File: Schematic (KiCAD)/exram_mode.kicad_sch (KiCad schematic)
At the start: 61 parts

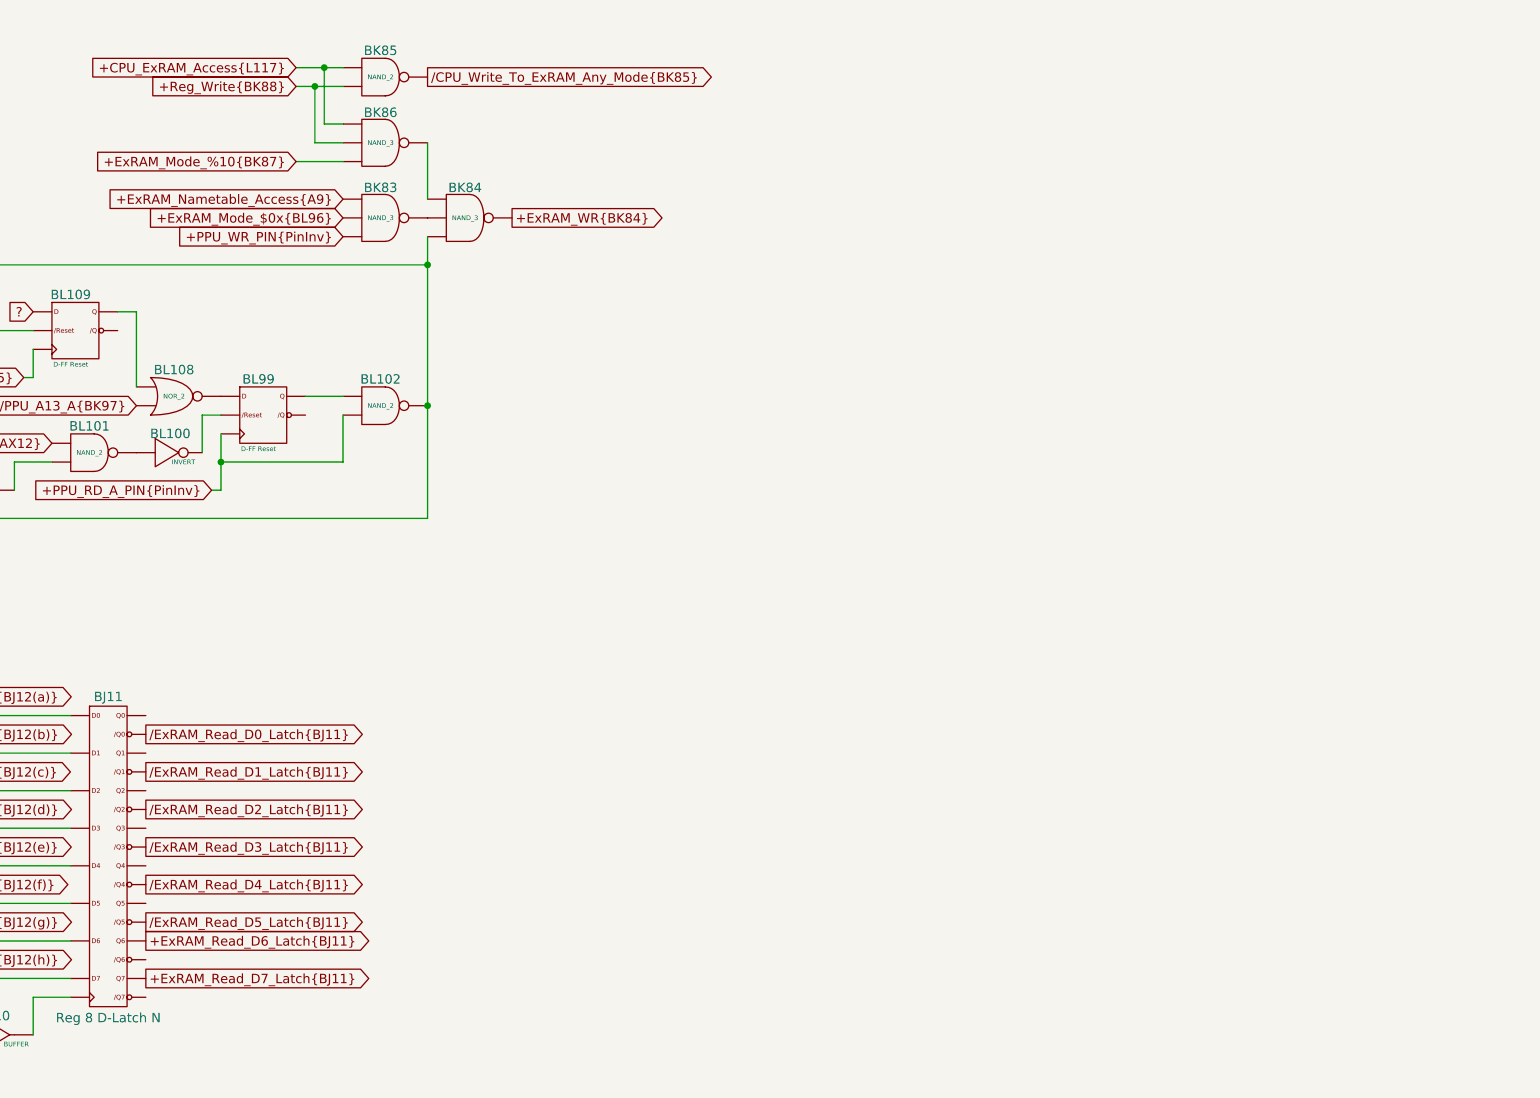
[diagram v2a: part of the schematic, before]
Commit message: - All cells in the left and center areas have now been added into the schematics.  - Changed naming of the PDF files; I was accidentally writing over furrtek's original with my new PDF.
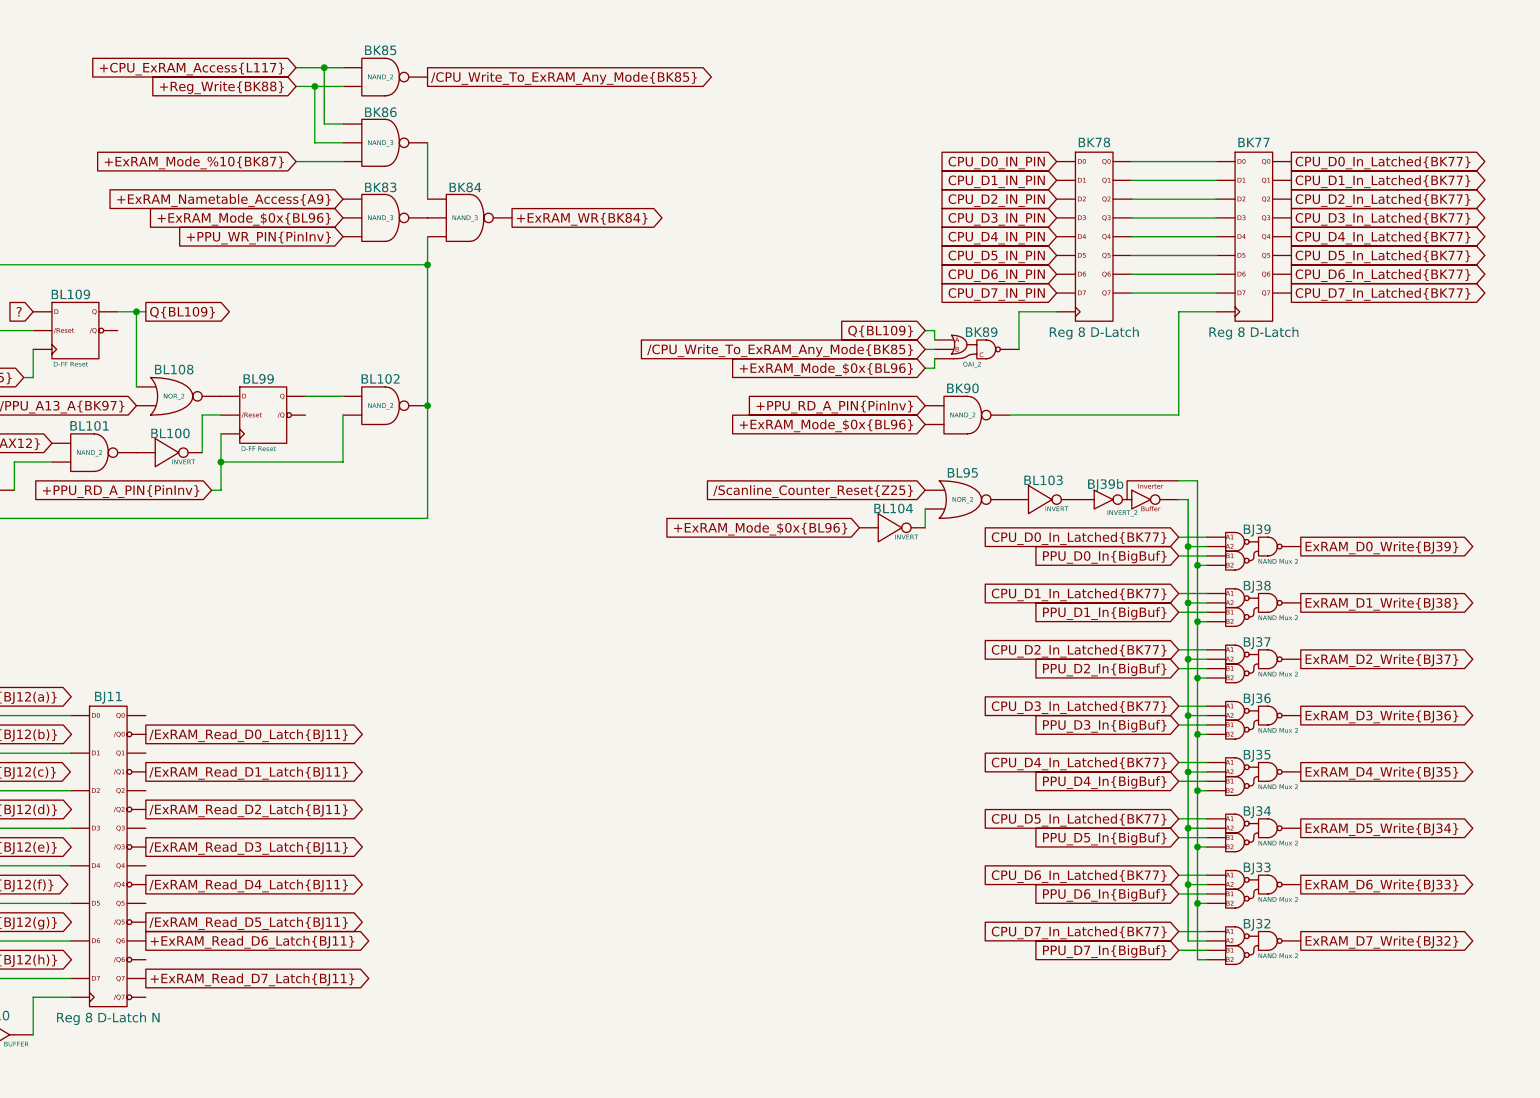
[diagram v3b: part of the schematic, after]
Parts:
- added BJ32, BJ33, BJ34, BJ35, BJ36, BJ37, BJ38, BJ39: NAND Mux 2, symbol MMC5:NAND_Mux_2
- added BJ39b: INVERT_2, symbol MMC5:INVERT_2
- added BK77, BK78: Reg 8 D-Latch, symbol MMC5:Reg_8_D-Latch
- added BK89: OAI_2, symbol MMC5:OAI_2
- added BK90: NAND_2, symbol MMC5:NAND_2
- added BL103, BL104: INVERT, symbol MMC5:INVERT
- added BL95: NOR_2, symbol MMC5:NOR_2
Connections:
- net +ExRAM_Mode_$0x{BL96}: now also BK89. (X), BK90. (X), BL104. (X)
- net +PPU_RD_A_PIN{PinInv}: now also BK90. (X)
- net CPU_D0_IN_PIN: now also BK78. (Q7)
- net CPU_D1_IN_PIN: now also BK78. (Q7)
- net /CPU_Write_To_ExRAM_Any_Mode{BK85}: now also BK89. (X)
- net at BL100. (X): now also BL101. (X); no longer BL99. (/Q)
- net at BL90. (X): now also BL91. (X); no longer BL89. (/Q)
- net at BL93. (X): now also BL92. (X); no longer BN2. (X)
- net at BJ10. (X): now also BJ11. (/Q7); no longer BJ9. (X)
- net at BL88. (X): now also BL86. (X); no longer BL84. (X)
- net at BL92. (X): now also BL94. (X); no longer BL93. (X)
- net at BM9. (X): now also BM10. (X); no longer BM8. (X)
- net at BM10. (X): now also BL91. (X); no longer BM9. (X)
- net at BL84. (X): now also BL85. (X); no longer BL87. (X)
- net at BL85. (X): now also BL86. (X); no longer BL82. (X)
- net at BM3. (X): now also BM4. (X); no longer BM2. (X)
- net at BM4. (X): now also BM5. (X); no longer BM3. (X)
- net at BL106. (X): now also BL109. (/Q); no longer BL105. (X)
- new net: BL81. (X), BL87. (X)
- new net: BK78. (Q7), BK89. (X)
- new net: BK84. (X), BL102. (X), BL105. (X), BL107. (X), BN3. (X), BN4. (X)
- new net: BK83. (X), BK84. (X)
- new net: BK84. (X), BK86. (X)
- new net: BL102. (X), BL99. (/Q)
- new net: BL108. (X), BL99. (/Q)
- new net: BL100. (X), BL99. (/Q)
- new net: BL93. (X), BL94. (X), BL98. (/Q)
- new net: BL98. (/Q), BN1. (X)
- new net: BK77. (Q7), BK90. (X)
- new net: BK77. (Q7), BK78. (Q7) (x8)
- new net: BK79. (X), BK81. (X), BK82. (Q1)
- new net: BL89. (/Q), BL90. (X)
- new net: BL93. (X), BN2. (X)
- new net: BJ7. (X), BJ9. (X)
- new net: BJ10. (X), BJ9. (X)
- new net: BJ32. (X), BJ33. (X), BJ34. (X), BJ35. (X), BJ36. (X), BJ37. (X), BJ38. (X), BJ39. (X), BJ39b. (X) (x2)
- new net: BL84. (X), BL88. (X)
- new net: BL88. (X), BM5. (X), BM6. (X)
- new net: BM8. (X), BM9. (X)
- new net: BK79. (X), BK82. (Q1), BL96. (X)
- new net: BL84. (X), BL87. (X)
- new net: BL104. (X), BL95. (X)
- new net: BL103. (X), BL95. (X)
- new net: BL82. (X), BL85. (X)
- new net: BL83. (X), BL84. (X)
- new net: BM2. (X), BM3. (X)
- new net: BK80. (X), BK82. (Q1)
- new net: BL105. (X), BL106. (X)
- new net: BL91. (X), BL92. (X)
- new net: BJ39b. (X), BL103. (X)
- new net CPU_D0_In_Latched{BK77}: BJ39. (X), BK77. (Q7)
- new net CPU_D1_In_Latched{BK77}: BJ38. (X), BK77. (Q7)
- new net CPU_D2_IN_PIN: BK78. (Q7)
- new net CPU_D2_In_Latched{BK77}: BJ37. (X), BK77. (Q7)
- new net CPU_D3_IN_PIN: BK78. (Q7)
- new net CPU_D3_In_Latched{BK77}: BJ36. (X), BK77. (Q7)
- new net CPU_D4_IN_PIN: BK78. (Q7)
- new net CPU_D4_In_Latched{BK77}: BJ35. (X), BK77. (Q7)
- new net CPU_D5_IN_PIN: BK78. (Q7)
- new net CPU_D5_In_Latched{BK77}: BJ34. (X), BK77. (Q7)
- new net CPU_D6_IN_PIN: BK78. (Q7)
- new net CPU_D6_In_Latched{BK77}: BJ33. (X), BK77. (Q7)
- new net CPU_D7_IN_PIN: BK78. (Q7)
- new net CPU_D7_In_Latched{BK77}: BJ32. (X), BK77. (Q7)
- new net ExRAM_D0_Write{BJ39}: BJ39. (X)
- new net ExRAM_D1_Write{BJ38}: BJ38. (X)
- new net ExRAM_D2_Write{BJ37}: BJ37. (X)
- new net ExRAM_D3_Write{BJ36}: BJ36. (X)
- new net ExRAM_D4_Write{BJ35}: BJ35. (X)
- new net ExRAM_D5_Write{BJ34}: BJ34. (X)
- new net ExRAM_D6_Write{BJ33}: BJ33. (X)
- new net ExRAM_D7_Write{BJ32}: BJ32. (X)
- new net PPU_D0_In{BigBuf}: BJ39. (X)
- new net PPU_D1_In{BigBuf}: BJ38. (X)
- new net PPU_D2_In{BigBuf}: BJ37. (X)
- new net PPU_D3_In{BigBuf}: BJ36. (X)
- new net PPU_D4_In{BigBuf}: BJ35. (X)
- new net PPU_D5_In{BigBuf}: BJ34. (X)
- new net PPU_D6_In{BigBuf}: BJ33. (X)
- new net PPU_D7_In{BigBuf}: BJ32. (X)
- new net Q{BL109}: BK89. (X), BL108. (X), BL109. (/Q)
- new net /Scanline_Counter_Reset{Z25}: BL95. (X)
